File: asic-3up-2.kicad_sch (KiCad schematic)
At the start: 81 parts, among them U11 MCP1824T-1202E/OT, U16 MCP1824T-1202E/OT, U17 MCP1824T-1202E/OT, U18 MCP1824T-0802E, U19 MCP1824T-0802E, U20 MCP1824T-0802E, U21 BM1362AC_MODE1, U22 BM1362AC_MODE0, U23 BM1362AC_MODE1

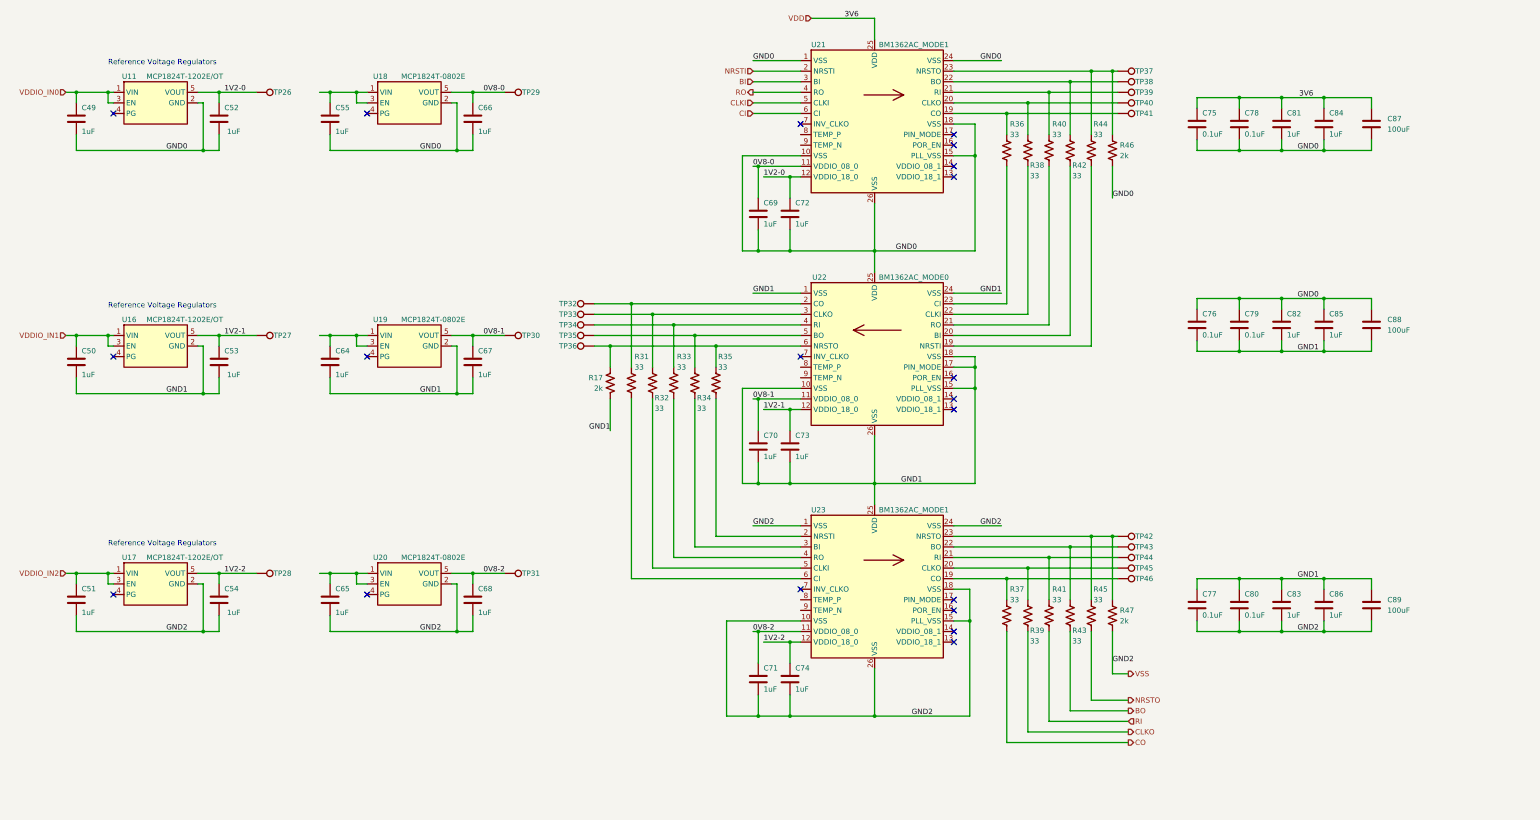
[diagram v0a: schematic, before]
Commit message: added all the ASICs to the schematic. added the RP2040 circuit for data. added the VDDIO boost circuit. schematic cleanup
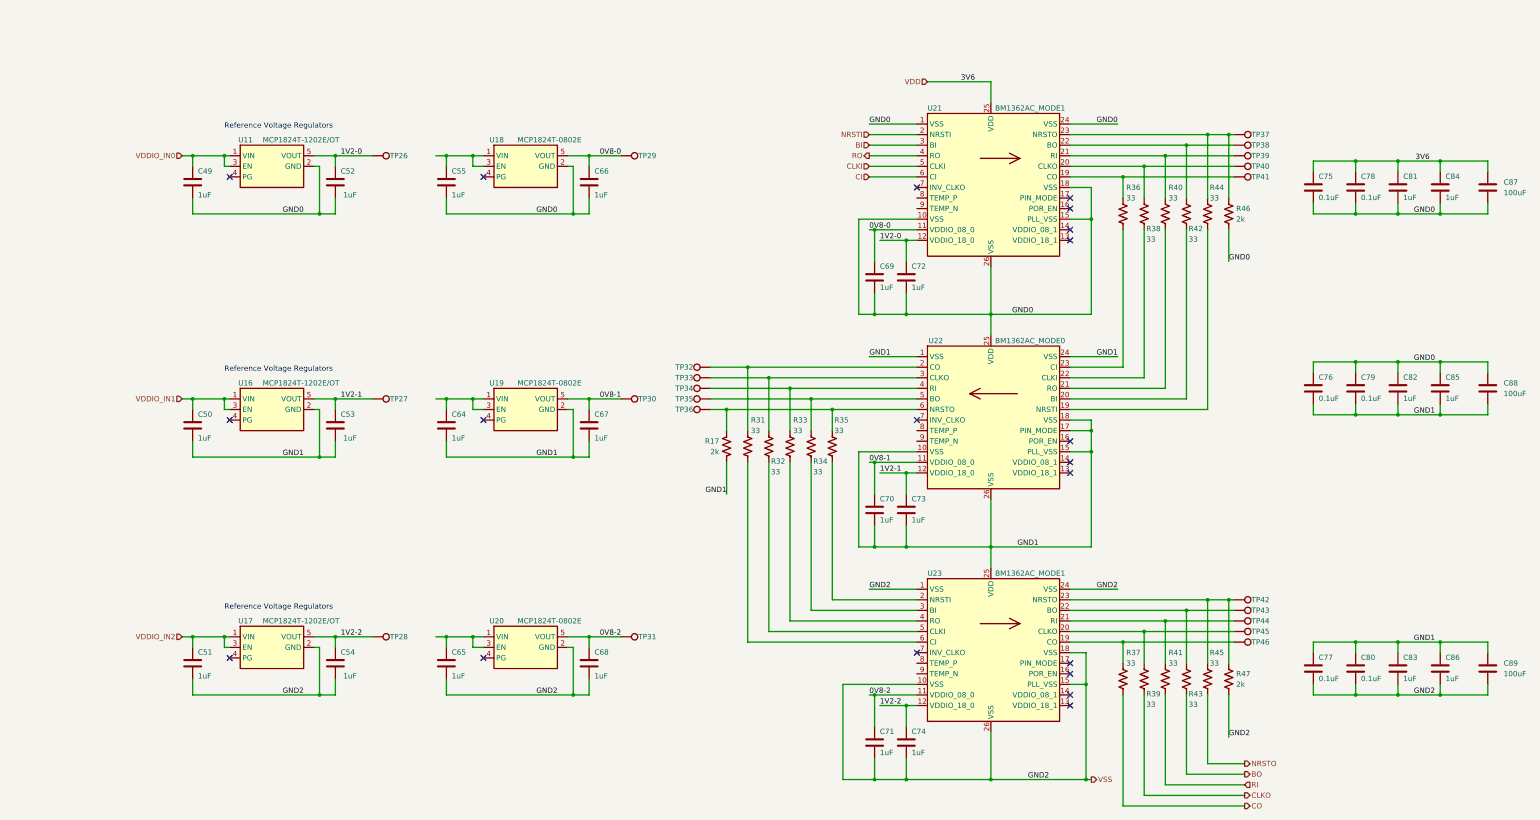
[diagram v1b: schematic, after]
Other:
- moved on the sheet: C49, C50, C51, C52, C53, C54, C55, C64, C65, C66, C67, C68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

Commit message: added sweet logo to schematic worksheet. Schematic cleanup.
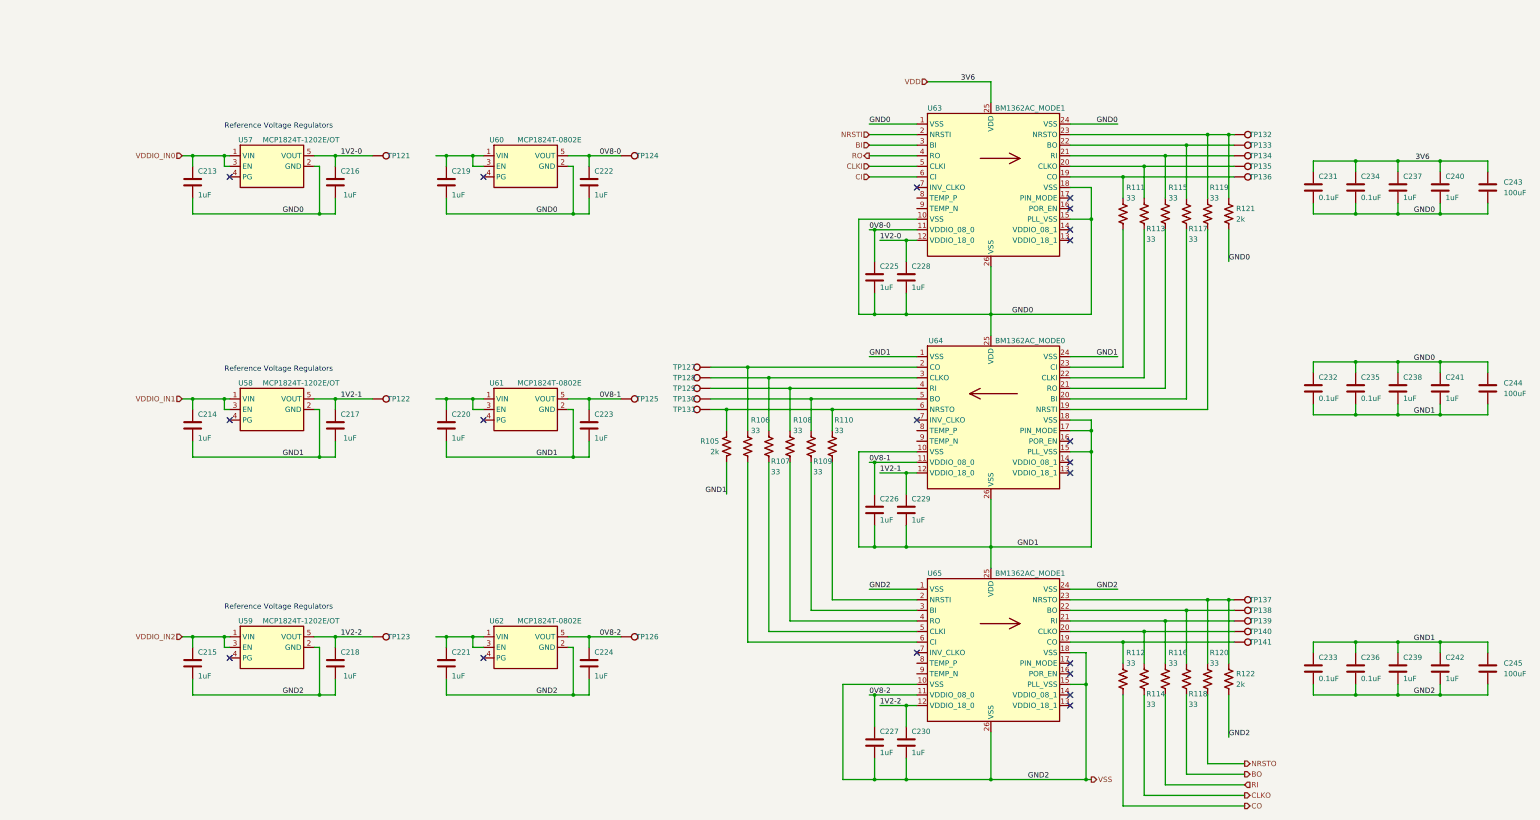
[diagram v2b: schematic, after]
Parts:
- renumbered C49 to C213, C50 to C214, C51 to C215, C52 to C216, C53 to C217, C54 to C218, C55 to C219, C64 to C220, C65 to C221, C66 to C222, C67 to C223, C68 to C224, C69 to C225, C70 to C226, C71 to C227, C72 to C228, C73 to C229, C74 to C230, C75 to C231, C76 to C232, C77 to C233, C78 to C234, C79 to C235, C80 to C236, C81 to C237, C82 to C238, C83 to C239, C84 to C240, C85 to C241, C86 to C242, C87 to C243, C88 to C244, C89 to C245, R17 to R105, R31 to R106, R32 to R107, R33 to R108, R34 to R109, R35 to R110, R36 to R111, R37 to R112, R38 to R113, R39 to R114, R40 to R115, R41 to R116, R42 to R117, R43 to R118, R44 to R119, R45 to R120, R46 to R121, R47 to R122, TP26 to TP121, TP27 to TP122, TP28 to TP123, TP29 to TP124, TP30 to TP125, TP31 to TP126, TP32 to TP127, TP33 to TP128, TP34 to TP129, TP35 to TP130, TP36 to TP131, TP37 to TP132, TP38 to TP133, TP39 to TP134, TP40 to TP135, TP41 to TP136, TP42 to TP137, TP43 to TP138, TP44 to TP139, TP45 to TP140, TP46 to TP141, U11 to U57, U16 to U58, U17 to U59, U18 to U60, U19 to U61, U20 to U62, U21 to U63, U22 to U64, U23 to U65

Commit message: starting layout
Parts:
- added J8, J9: Conn_01x01, emberone:5x9_powertab, symbol Connector_Generic:Conn_01x01
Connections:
- net GND0: now also J8.1 (Pin_1)
- net GND1: now also J9.1 (Pin_1)
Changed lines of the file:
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@@
 	)
 	(junction
+		(at 248.92 97.79)
+		(diameter 0)
+		(color 0 0 0 0)
+	)
+	(junction
 		(at 91.44 123.19)
 		(diameter 0.9144)
@@
 	)
 	(junction
+		(at 248.92 153.67)
+		(diameter 0)
+		(color 0 0 0 0)
+	)
+	(junction
 		(at 210.82 125.73)
 		(diameter 0)
@@
 	(wire
 		(pts
-			(xy 248.92 91.44) (xy 248.92 102.87)
+			(xy 248.92 91.44) (xy 248.92 97.79)
 		)
 		(stroke
@@
 	(wire
 		(pts
-			(xy 248.92 147.32) (xy 248.92 158.75)
+			(xy 248.92 147.32) (xy 248.92 153.67)
 		)
 		(stroke
@@
 	(wire
 		(pts
+			(xy 248.92 153.67) (xy 248.92 158.75)
+		)
+		(stroke
+			(width 0)
+			(type default)
+		)
+	)
+	(wire
+		(pts
+			(xy 248.92 97.79) (xy 248.92 102.87)
+		)
+		(stroke
+			(width 0)
+			(type default)
+		)
+	)
+	(wire
+		(pts
 			(xy 273.05 158.75) (xy 273.05 135.89)
 		)
@@
 	)
 	(symbol
+		(lib_id "Connector_Generic:Conn_01x01")
+		(at 254 97.79 0)
+		(unit 1)
+		(exclude_from_sim no)
+		(in_bom yes)
+		(on_board yes)
+		(dnp no)
+		(property "Reference" "J8"
+			(at 256.286 97.79 0)
+			(effects
+				(font
+					(size 1.27 1.27)
+				)
+				(justify left)
+			)
+		)
+		(property "Value" "Conn_01x01"
+			(at 256.54 99.0599 0)
+			(effects
+				(font
+					(size 1.27 1.27)
+				)
+				(justify left)
+				(hide yes)
+			)
+		)
+		(property "Footprint" "emberone:5x9_powertab"
+			(at 254 97.79 0)
+			(effects
+				(font
+					(size 1.27 1.27)
+				)
+				(hide yes)
+			)
+		)
+		(property "Datasheet" "~"
+			(at 254 97.79 0)
+			(effects
+				(font
+					(size 1.27 1.27)
+				)
+				(hide yes)
+			)
+		)
+		(property "Description" "powertab"
+			(at 254 97.79 0)
+			(effects
+				(font
+					(size 1.27 1.27)
+				)
+				(hide yes)
+			)
+		)
+		(pin "1"
+		)
+		(instances
+			(project "emberone"
+				(path "/b036224c-4cdf-48cc-81df-19bc5283ebd2/b7ad7cc6-371f-46f9-875b-8b04bdc75b20"
+					(reference "J8")
+					(unit 1)
+				)
+			)
+		)
+	)
+	(symbol
 		(lib_id "Connector:TestPoint")
 		(at 307.34 62.23 270)
@@
 					(unit 1)
 				)
+			)
+		)
+	)
+	(symbol
+		(lib_id "Connector_Generic:Conn_01x01")
+		(at 254 153.67 0)
+		(unit 1)
+		(exclude_from_sim no)
+		(in_bom yes)
+		(on_board yes)
+		(dnp no)
+		(property "Reference" "J9"
+			(at 256.286 153.67 0)
+			(effects
+				(font
+					(size 1.27 1.27)
+				)
+				(justify left)
+			)
+		)
+		(property "Value" "Conn_01x01"
+			(at 256.54 154.9399 0)
+			(effects
+				(font
+					(size 1.27 1.27)
+				)
+				(justify left)
+				(hide yes)
+			)
+		)
+		(property "Footprint" "emberone:5x9_powertab"
+			(at 254 153.67 0)
+			(effects
+				(font
+					(size 1.27 1.27)
+				)
+				(hide yes)
+			)
+		)
+		(property "Datasheet" "~"
+			(at 254 153.67 0)
+			(effects
+				(font
+					(size 1.27 1.27)
+				)
+				(hide yes)
+			)
+		)
+		(property "Description" "powertab"
+			(at 254 153.67 0)
+			(effects
+				(font
+					(size 1.27 1.27)
+				)
+				(hide yes)
+			)
+		)
+		(pin "1"
+		)
+		(instances
+			(project "emberone"
+				(path "/b036224c-4cdf-48cc-81df-19bc5283ebd2/b7ad7cc6-371f-46f9-875b-8b04bdc75b20"
+					(reference "J9")
+					(unit 1)
+				)

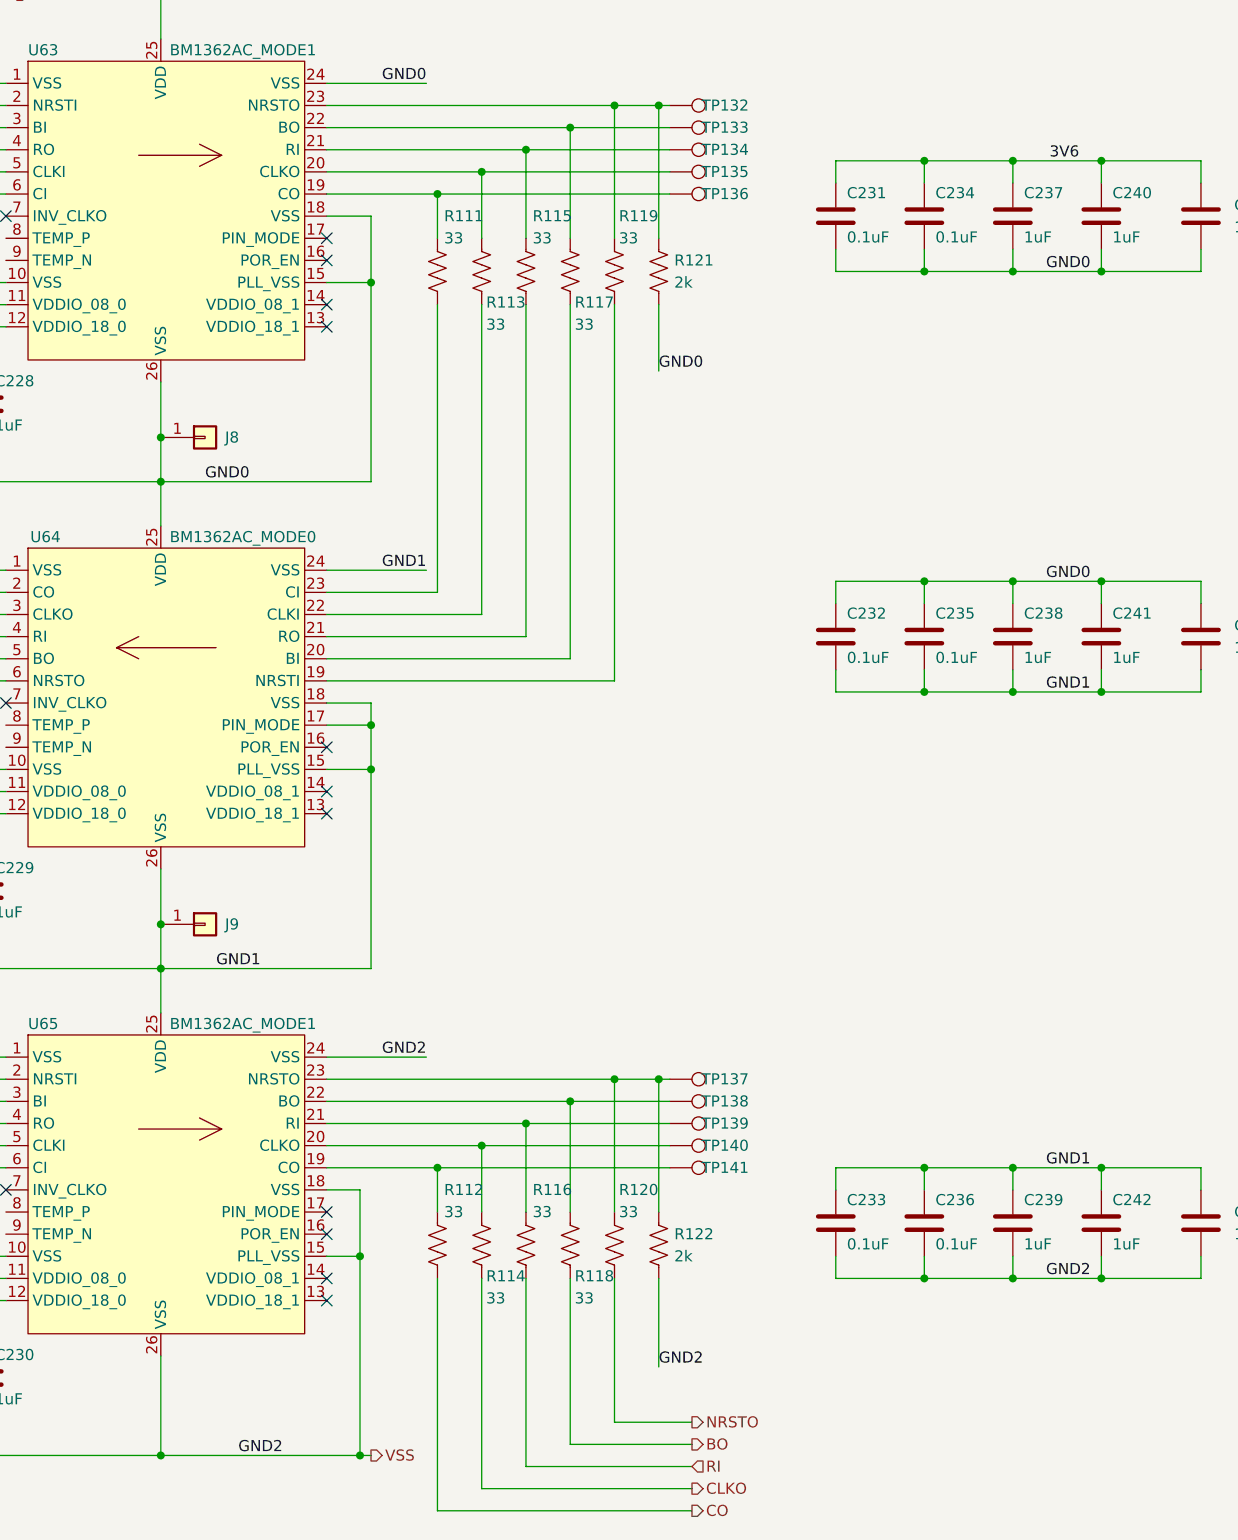
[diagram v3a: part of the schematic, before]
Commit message: so much placing. added mask and paste opening on ASIC footprints. added a pad for a rear heatsink
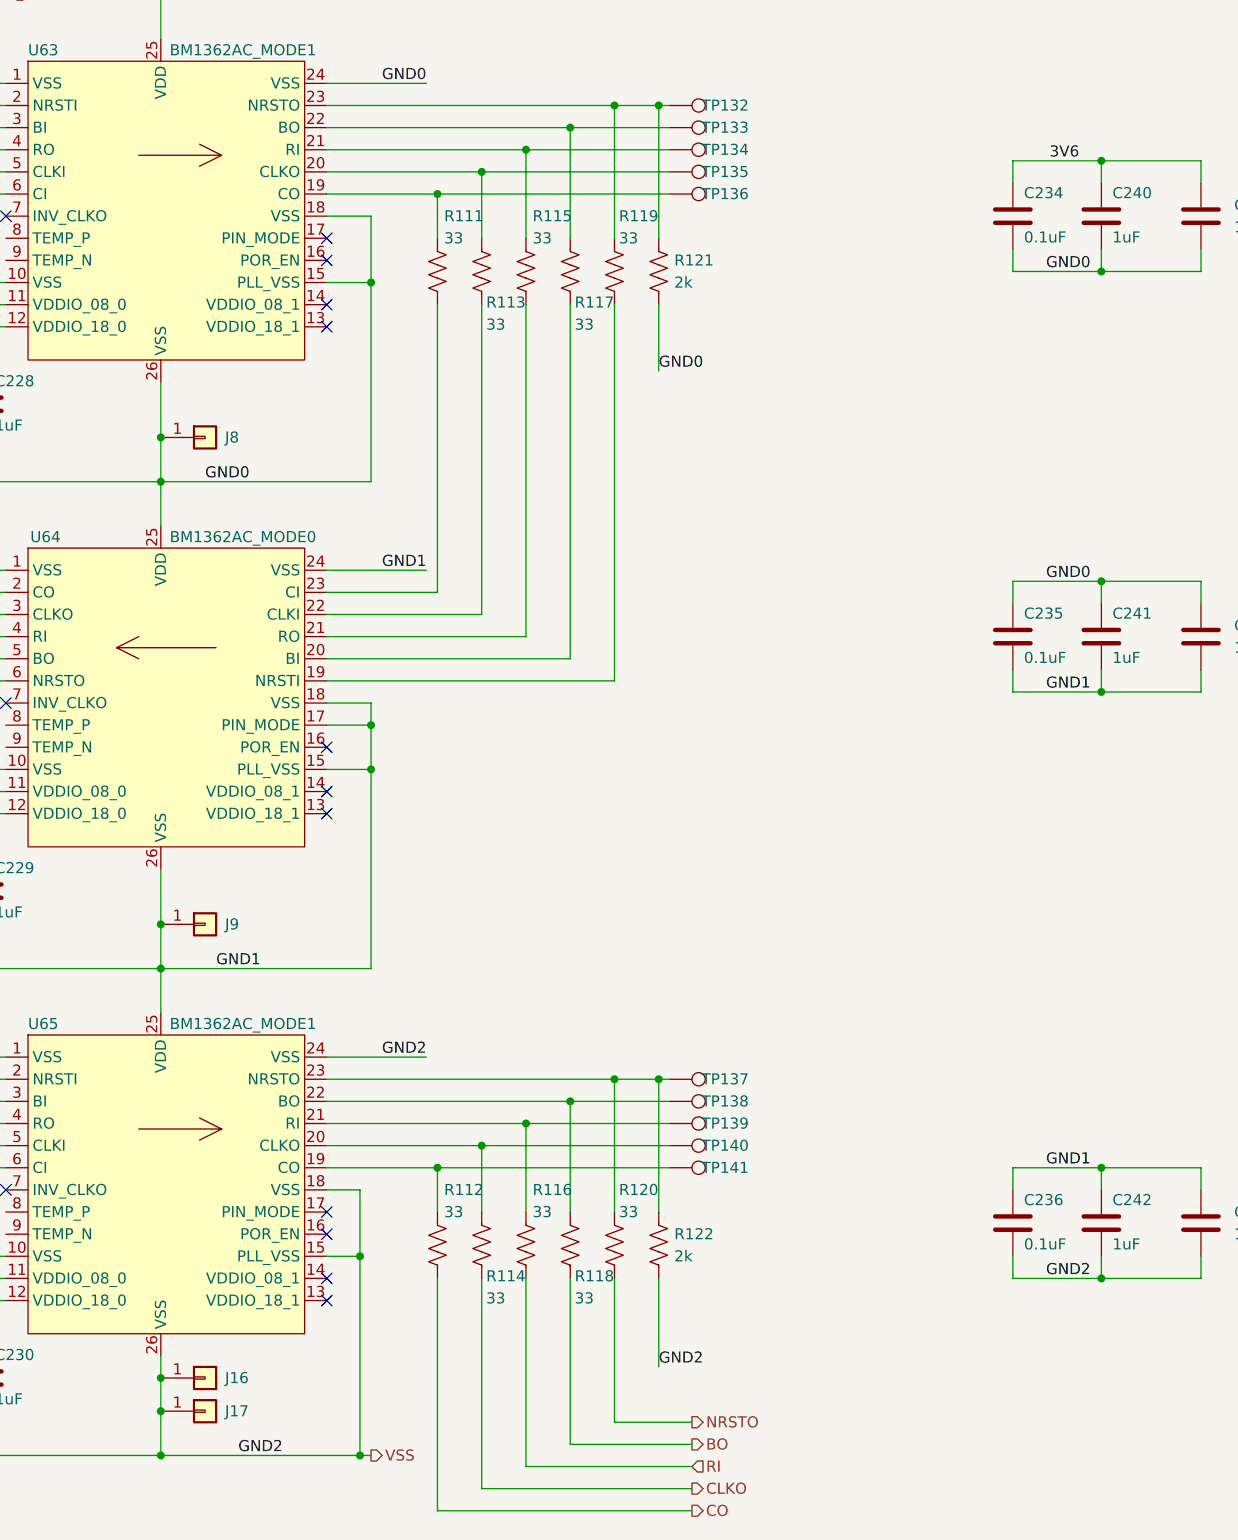
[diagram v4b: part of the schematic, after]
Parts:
- removed C231, C232, C233: 0.1uF, Capacitor_SMD:C_0402_1005Metric, symbol Device:C
- removed C237, C238, C239: 1uF, Capacitor_SMD:C_0402_1005Metric, symbol Device:C
- added J16: Conn_01x01, emberone:14x9_powertab_L, symbol Connector_Generic:Conn_01x01
- added J17: Conn_01x01, emberone:14x9_powertab_R, symbol Connector_Generic:Conn_01x01
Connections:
- net VSS: now also J16.1 (Pin_1), J17.1 (Pin_1)
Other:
- moved on the sheet: C234, C235, C236
